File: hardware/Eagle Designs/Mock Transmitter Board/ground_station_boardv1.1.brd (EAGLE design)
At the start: 3 parts, among them J1 MCX-J-P-H-RA-TH1, U1 RFM23BP

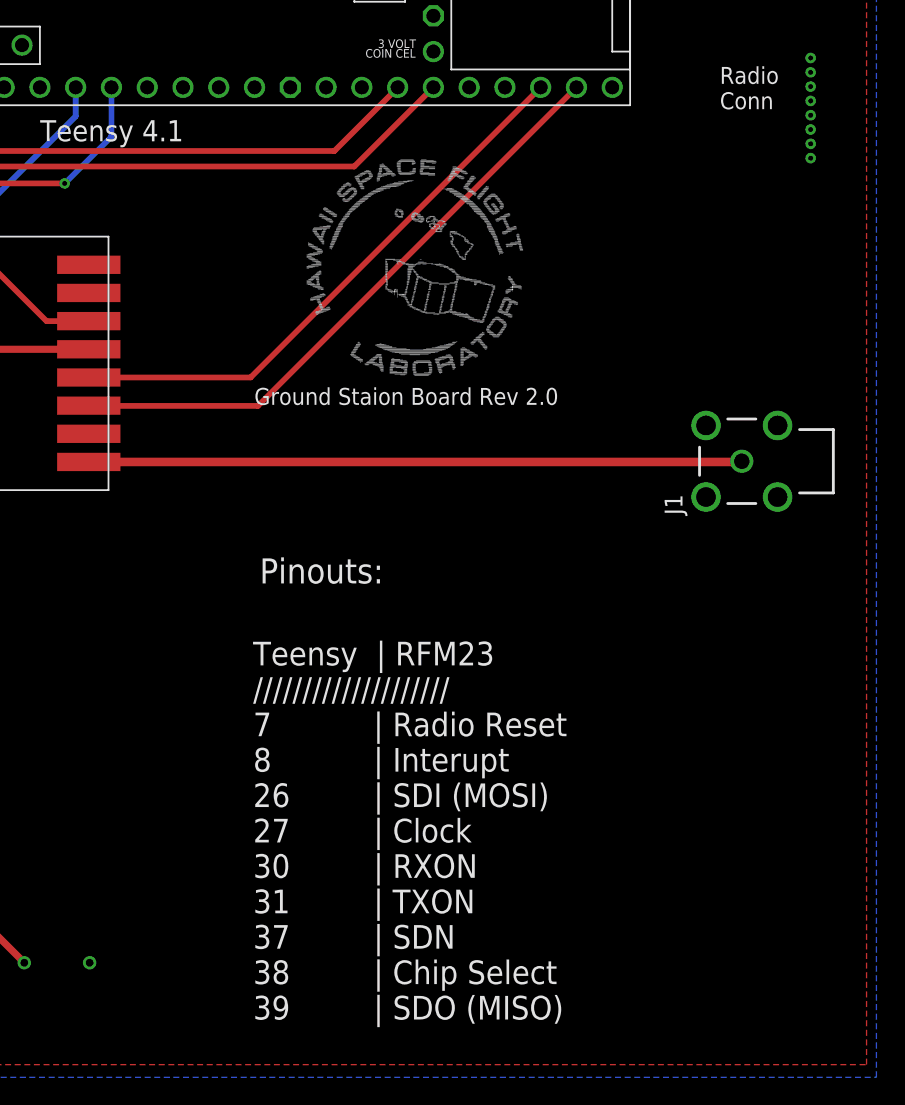
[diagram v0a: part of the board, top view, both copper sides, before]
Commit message: Swapped the antenna pad for the MCX connector on the ground station board. Created the mock transmission board which is a radio, teensy and antenna.
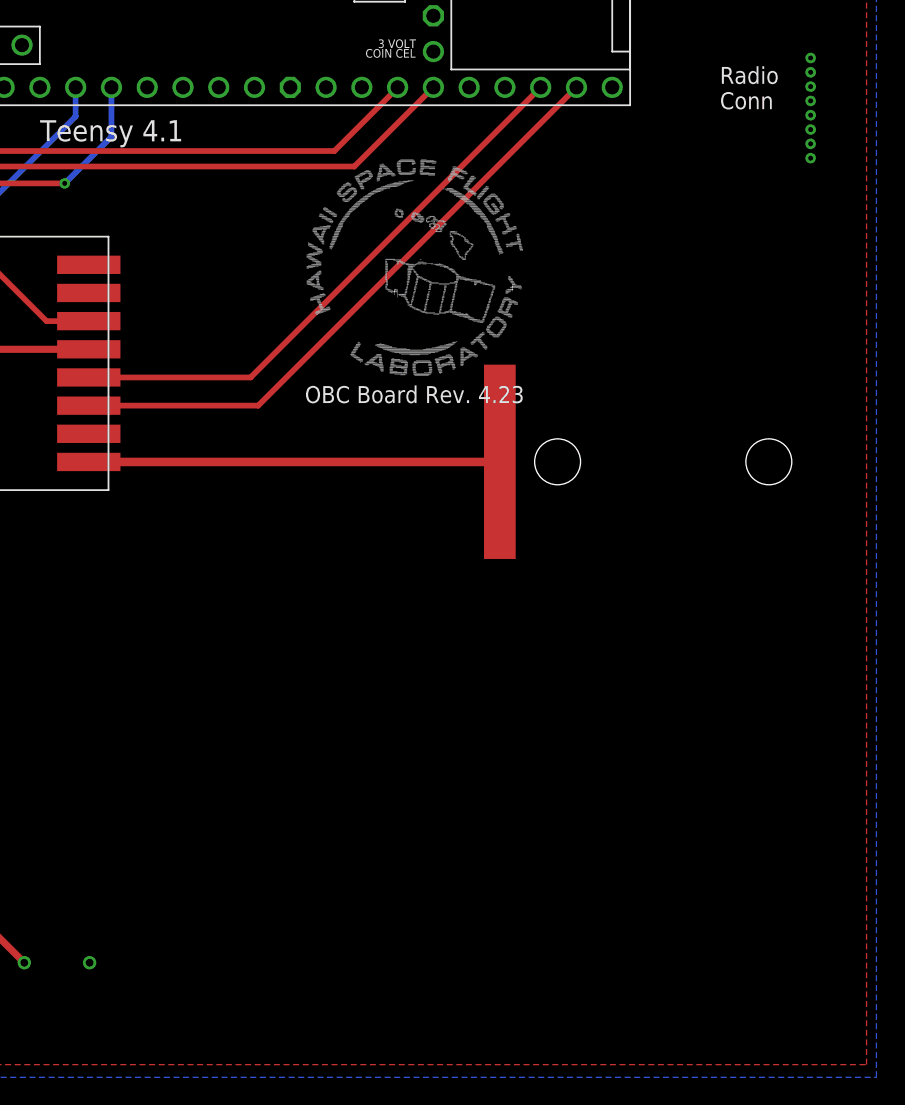
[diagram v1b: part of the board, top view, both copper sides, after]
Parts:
- removed J1: MCX-J-P-H-RA-TH1, OBCv4:SAMTEC_MCX-J-P-H-RA-TH1
- added U$2: ANTENNA_PAD+HOLES, Antenna_Pad:ANTENNA_PAD+HOLES
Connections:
- net N$1: now also U$2.1; no longer J1.1
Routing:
- net N$1: track 46.4 -> 29.2 mm
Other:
- board text added: "OBC Board Rev. 4.23"
- board text removed: "Ground Staion Board Rev 2.0"
- board text removed: "Pinouts:"
- board text removed: "Teensy | RFM23 //////////////////// 7 | Radio Reset 8 | Interupt 26 | SDI (MOSI) 27 | Clock 30 | RXON 31 | TXON 37 | SDN 38 | Chip Select 39 | SDO (MISO)"
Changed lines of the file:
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@@
 <fusionsync huburn="a.YnVzaW5lc3M6aGF3YWlpMzk3" projecturn="a.YnVzaW5lc3M6aGF3YWlpMzk3I0QyMDIxMDIxMTM4MTc0NzIyNg" f3durn="urn:adsk.wipprod:dm.lineage:WPvLawa_Q36ULf1lFy3S-g" pcbguid="" lastpulledtime="" lastsyncedchangeguid="" latestrevisionid="935d8412-0a8b-471e-9db4-d59a038692ee" lastsyncedrevisionid="935d8412-0a8b-471e-9db4-d59a038692ee" lastboardhashguid="5ede64c8-f60e-0077-9b9e-ecb65980b17f" lastpushedtime="2021-09-29T01:22:19Z" linktopcb3d="false"/>
 <plain>
-<text x="49.0388" y="41.564" size="1.2" layer="25" font="vector">Ground Staion Board Rev 2.0</text>
+<text x="52.6288" y="41.694" size="1.2" layer="25" font="vector">OBC Board Rev. 4.23</text>
 <rectangle x1="60.5079" y1="43.6237" x2="61.4223" y2="43.6491" layer="21"/>
 <rectangle x1="60.4317" y1="43.6237" x2="60.5079" y2="43.6491" layer="21"/>
@@
 <text x="82.1" y="62.56" size="1.2" layer="25" font="vector">Radio
 Conn</text>
-<text x="49.4188" y="28.884" size="1.778" layer="25" font="vector">Pinouts:</text>
-<text x="48.9588" y="-4.596" size="1.6764" layer="25" font="vector">Teensy  | RFM23
-////////////////////
-7           | Radio Reset
-8           | Interupt
-26         | SDI (MOSI)
-27         | Clock
-30         | RXON
-31         | TXON
-37         | SDN
-38         | Chip Select
-39         | SDO (MISO)
-</text>
 </plain>
 <attributes>
@@
 <attribute name="VALUE" x="5.3767" y="33.7567" size="1.77858125" layer="27"/>
 </element>
-<element name="J1" library="OBCv4" package="SAMTEC_MCX-J-P-H-RA-TH1" value="MCX-J-P-H-RA-TH1" x="83.66" y="37.56" smashed="yes" rot="R90">
-<attribute name="DESCRIPTION" value=" MCX Connector Jack, Female Socket 50Ohm Through Hole, Right Angle Solder " x="68.94" y="29.36" size="1.778" layer="27" rot="R90" display="off"/>
-<attribute name="DIGI-KEY_PART_NUMBER" value="SAM10607-ND" x="68.94" y="29.36" size="1.778" layer="27" rot="R90" display="off"/>
-<attribute name="MF" value="Samtec" x="68.94" y="29.36" size="1.778" layer="27" rot="R90" display="off"/>
-<attribute name="MP" value="MCX-J-P-H-RA-TH1" x="68.94" y="29.36" size="1.778" layer="27" rot="R90" display="off"/>
-<attribute name="NAME" x="79.45" y="33.75" size="1.27" layer="25" rot="R90"/>
-<attribute name="PACKAGE" value="None" x="68.94" y="29.36" size="1.778" layer="27" rot="R90" display="off"/>
-<attribute name="PURCHASE-URL" value="https://pricing.snapeda.com/search/part/MCX-J-P-H-RA-TH1/?ref=eda" x="68.94" y="29.36" size="1.778" layer="27" rot="R90" display="off"/>
-<attribute name="VALUE" x="90.645" y="33.75" size="1.27" layer="27" rot="R90" align="top-left"/>
-</element>
+<element name="U$2" library="Antenna_Pad" package="ANTENNA_PAD+HOLES" value="ANTENNA_PAD+HOLES" x="78.08" y="37.52" smashed="yes" rot="R270"/>
 </elements>
 <signals>
@@
 <contactref element="U$1" pad="31-CTX3"/>
 <contactref element="U1" pad="11"/>
-<wire x1="37.29" y1="41.51" x2="37.31" y2="41.49" width="0.4064" layer="1"/>
-<wire x1="49.3" y1="41.49" x2="37.31" y2="41.49" width="0.4064" layer="1"/>
-<wire x1="49.3" y1="41.49" x2="71.92" y2="64.11" width="0.4064" layer="1"/>
+<wire x1="37.29" y1="41.51" x2="49.32" y2="41.51" width="0.4064" layer="1"/>
+<wire x1="49.32" y1="41.51" x2="71.92" y2="64.11" width="0.4064" layer="1"/>
 </signal>
 <signal name="SDN">
@@
 </signal>
 <signal name="N$1">
-<contactref element="J1" pad="1"/>
+<contactref element="U$2" pad="1"/>
 <contactref element="U1" pad="9"/>
-<wire x1="83.61" y1="37.51" x2="83.66" y2="37.56" width="0.1524" layer="1"/>
-<wire x1="37.29" y1="37.51" x2="83.61" y2="37.51" width="0.6096" layer="1"/>
+<wire x1="37.29" y1="37.51" x2="66.47" y2="37.51" width="0.6096" layer="1"/>
+<wire x1="66.47" y1="37.51" x2="66.48" y2="37.52" width="0.6096" layer="1"/>
 </signal>
 </signals>
